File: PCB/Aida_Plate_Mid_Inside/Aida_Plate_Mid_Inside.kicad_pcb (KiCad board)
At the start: 2 copper layers, 50.3 x 61.6 mm, 8 parts

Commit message: プレート類調整中。LED位置検討中。
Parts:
- added H13: COL_L_4_from_Mid_Inside, Lib_Local:MountingHole_M2_Through-hole_tap_THC-0.8-2.0-2_minimal, F.Cu at (147.6, 73.8)
- added L1: SK6812MINI-E, Lib_Local:YS-SK6812MINI-E_middle_hole_with_small_pad, B.Cu at (142.9, 59.5)
- added L2: SK6812MINI-E, Lib_Local:YS-SK6812MINI-E_middle_hole_with_small_pad, B.Cu at (142.9, 64.3)
- added L3: SK6812MINI-E, Lib_Local:YS-SK6812MINI-E_middle_hole_with_small_pad, B.Cu at (142.9, 69.1)
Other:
- board size 50.3 x 61.6 mm -> 59.2 x 61.6 mm

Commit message: LED位置、とりあえず決定。
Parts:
- removed H13: COL_L_4_from_Mid_Inside, Lib_Local:MountingHole_M2_Through-hole_tap_THC-0.8-2.0-2_minimal
- removed L1, L2, L3: SK6812MINI-E, Lib_Local:YS-SK6812MINI-E_middle_hole_with_small_pad
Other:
- board size 59.2 x 61.6 mm -> 50.3 x 61.6 mm
- board text added: "DO NOT DRILL CIRCLES. Those are not holes."

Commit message: 原点ガイドを追加。基板Mid_InsideのLED穴形状調整
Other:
- board text added: "Center Origin"
- board text added: "Grid Origin"
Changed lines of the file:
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@@
 		(layer "Edge.Cuts")
+	)
+	(gr_circle
+		(center 23.8125 23.8125)
+		(end 25.003125 23.8125)
+		(stroke
+			(width 0.1)
+			(type default)
+		)
+		(fill no)
+		(layer "User.1")
+	)
+	(gr_line
+		(start 150.01875 23.8125)
+		(end 154.78125 23.8125)
+		(stroke
+			(width 0.1)
+			(type default)
+		)
+		(layer "User.1")
+	)
+	(gr_line
+		(start 23.8125 21.43125)
+		(end 23.8125 26.19375)
+		(stroke
+			(width 0.1)
+			(type default)
+		)
+		(layer "User.1")
+	)
+	(gr_line
+		(start 152.4 21.43125)
+		(end 152.4 26.19375)
+		(stroke
+			(width 0.1)
+			(type default)
+		)
+		(layer "User.1")
+	)
+	(gr_line
+		(start 21.43125 23.8125)
+		(end 26.19375 23.8125)
+		(stroke
+			(width 0.1)
+			(type default)
+		)
+		(layer "User.1")
+	)
+	(gr_circle
+		(center 152.4 23.8125)
+		(end 153.590625 23.8125)
+		(stroke
+			(width 0.1)
+			(type default)
+		)
+		(fill no)
+		(layer "User.1")
 	)
 	(gr_text "DO NOT DRILL CIRCLES.\nThose are not holes."
@@
 				(size 2 2)
 				(thickness 0.25)
+			)
+			(justify left bottom)
+		)
+	)
+	(gr_text "Grid Origin"
+		(at 20.240625 21.43125 0)
+		(layer "User.1")
+		(effects
+			(font
+				(size 1 1)
+				(thickness 0.15)
+			)
+			(justify left bottom)
+		)
+	)
+	(gr_text "Center Origin"
+		(at 148.828125 21.43125 0)
+		(layer "User.1")
+		(effects
+			(font
+				(size 1 1)
+				(thickness 0.15)
 			)
 			(justify left bottom)
@@
 		)
 	)
+	(group ""
+		(members "15531f46-542e-4131-8094-c3650f5a9374" "2cdf3d86-d72e-4109-b224-193631557260"
+			"ea616511-4593-4c1b-8940-5a7e35608ef3" "eb1049b0-75b3-4886-85d8-c5c06e918374"
+		)
+	)
+	(group ""
+		(members "05c20652-2754-4f66-9b43-a5211af0040d" "29cce3e9-f593-4843-b647-fa03b3cb47b6"
+			"51cdd694-2f4d-4852-8a7e-19bc042b84af" "cdfebcb0-57f7-4ed5-aca3-5b13bf482387"
+		)
+	)

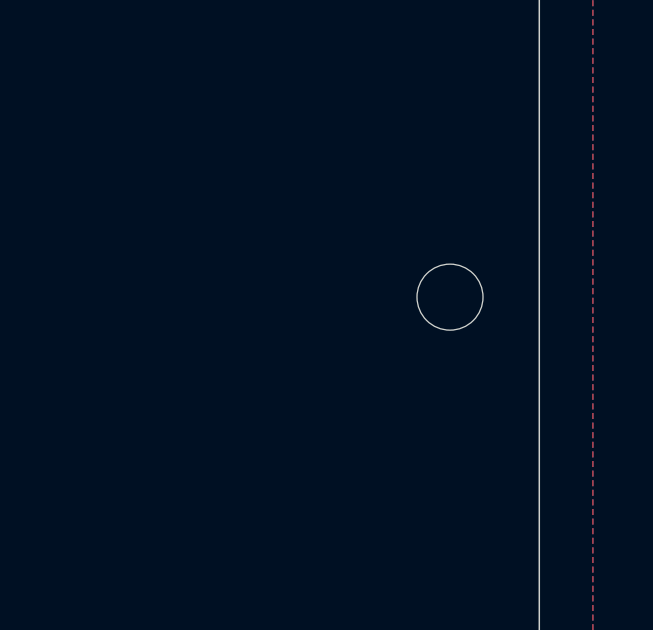
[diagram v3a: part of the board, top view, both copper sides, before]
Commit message: LEDを1/16u下へ移動。 右手のフラッシュメモリとの干渉回避のためボトムプレートの穴位置調整。
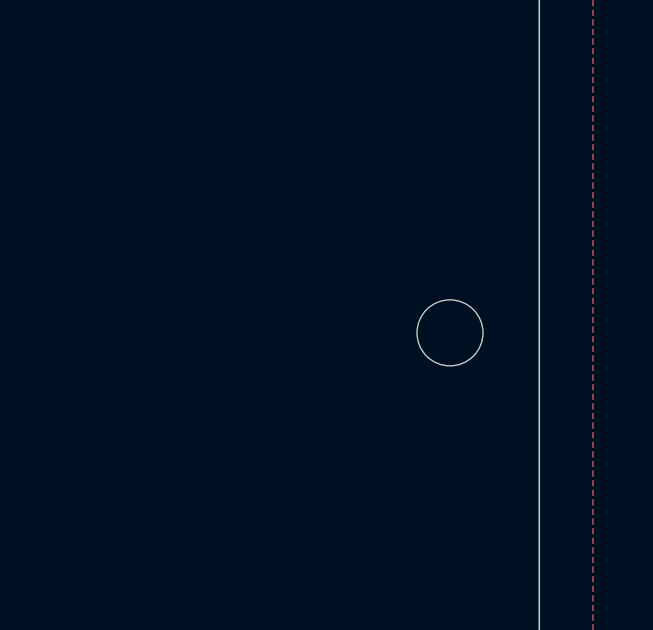
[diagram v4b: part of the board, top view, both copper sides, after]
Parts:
- moved H5 1.19 mm to (147.6, 75.0)
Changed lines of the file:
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@@
 	(footprint "Lib_Local:MountingHole_2.2mm_M2_minimal"
 		(layer "F.Cu")
-		(at 147.637604 73.818792)
+		(at 147.6375 75.009375)
 		(descr "Mounting Hole 2.2mm, M2, no annular, generated by kicad-footprint-generator mountinghole.py")
 		(tags "mountinghole M2")
@@
 	)
 	(gr_circle
-		(center 142.8751 69.056288)
-		(end 143.470413 69.056288)
+		(center 142.8751 70.246875)
+		(end 143.470413 70.246875)
 		(stroke
 			(width 0.1)
@@
 	)
 	(gr_circle
-		(center 142.8751 64.293784)
-		(end 143.470413 64.293784)
+		(center 142.875 65.484375)
+		(end 143.470313 65.484375)
 		(stroke
 			(width 0.1)
@@
 	)
 	(gr_circle
-		(center 142.8751 59.53128)
-		(end 143.470413 59.53128)
+		(center 142.875 60.721875)
+		(end 143.470313 60.721875)
 		(stroke
 			(width 0.1)
@@
 	)
 	(gr_circle
-		(center 142.8751 69.056288)
-		(end 143.470413 69.056288)
+		(center 142.8751 70.246875)
+		(end 143.470413 70.246875)
 		(stroke
 			(width 0.1)
@@
 	)
 	(gr_circle
-		(center 142.8751 64.293784)
-		(end 143.470413 64.293784)
+		(center 142.875 65.484375)
+		(end 143.470313 65.484375)
 		(stroke
 			(width 0.1)
@@
 	)
 	(gr_circle
-		(center 142.8751 59.53128)
-		(end 143.470413 59.53128)
+		(center 142.875 60.721875)
+		(end 143.470313 60.721875)
 		(stroke
 			(width 0.1)
@@
 	)
 	(gr_rect
-		(start 141.0866 67.56705)
-		(end 144.6584 70.54355)
+		(start 141.0866 68.758625)
+		(end 144.6584 71.735125)
 		(stroke
 			(width 0.1)
@@
 	(gr_arc
 		(start 150.614193 114.300068)
-		(mid 149.916814 115.98396)
+		(mid 149.916843 115.98399)
 		(end 148.232943 116.681318)
 		(stroke
@@
 	(gr_arc
 		(start 66.67506 116.681336)
-		(mid 64.570318 115.809534)
+		(mid 64.570283 115.80954)
 		(end 63.698497 113.704773)
 		(stroke
@@
 	)
 	(gr_rect
-		(start 141.0866 62.80465)
-		(end 144.6584 65.78115)
+		(start 141.0866 63.996225)
+		(end 144.6584 66.972725)
 		(stroke
 			(width 0.1)
@@
 	)
 	(gr_rect
-		(start 141.0866 58.04225)
-		(end 144.6584 61.01875)
+		(start 141.0866 59.233825)
+		(end 144.6584 62.210325)
 		(stroke
 			(width 0.1)
@@
 			(pts
 				(arc
-					(start 142.279787 59.530775)
-					(mid 143.470413 59.530775)
-					(end 142.279787 59.530775)
+					(start 142.279687 60.72137)
+					(mid 143.470313 60.72137)
+					(end 142.279687 60.72137)
 				)
 			)
@@
 			(pts
 				(arc
-					(start 142.279787 69.055783)
-					(mid 143.470413 69.055783)
-					(end 142.279787 69.055783)
+					(start 142.279787 70.24637)
+					(mid 143.470413 70.24637)
+					(end 142.279787 70.24637)
 				)
 			)
@@
 			(pts
 				(arc
-					(start 142.279787 64.293279)
-					(mid 143.470413 64.293279)
-					(end 142.279787 64.293279)
+					(start 142.279687 65.48387)
+					(mid 143.470313 65.48387)
+					(end 142.279687 65.48387)
 				)
 			)
